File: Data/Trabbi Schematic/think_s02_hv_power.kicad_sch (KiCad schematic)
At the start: 8 parts, among them K1 Start Inhibit Relay A, M1 Main Motor AC, SW1 Battery Lock Switch, SW2 Main Current Switch, U1 Contactor Box, U2 Motor Controller (TIM)

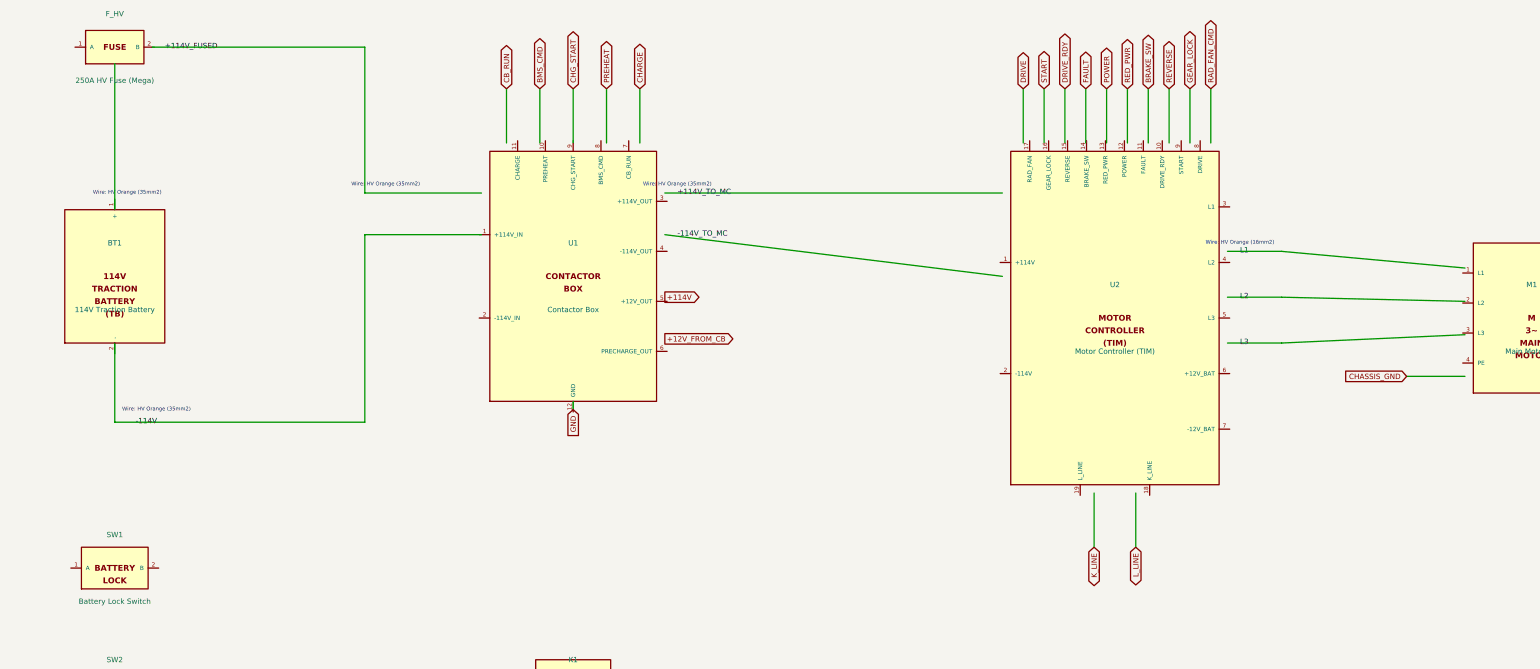
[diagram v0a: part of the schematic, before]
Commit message: Fix wire-to-pin connections: use exact calculated pin positions
Refactored gen_think_complete.py to compute exact pin schematic
coordinates instead of using approximate manual offsets. Added p()
method to Sheet class that transforms symbol-local pin positions to
schematic coordinates. All 232 wire calls across 13 sub-sheet
generators now use p() for pin endpoints, fixing misaligned
connections (previously off by 0.54-10+ units).

Co-Authored-By: Claude Opus 4.6 <noreply@anthropic.com>
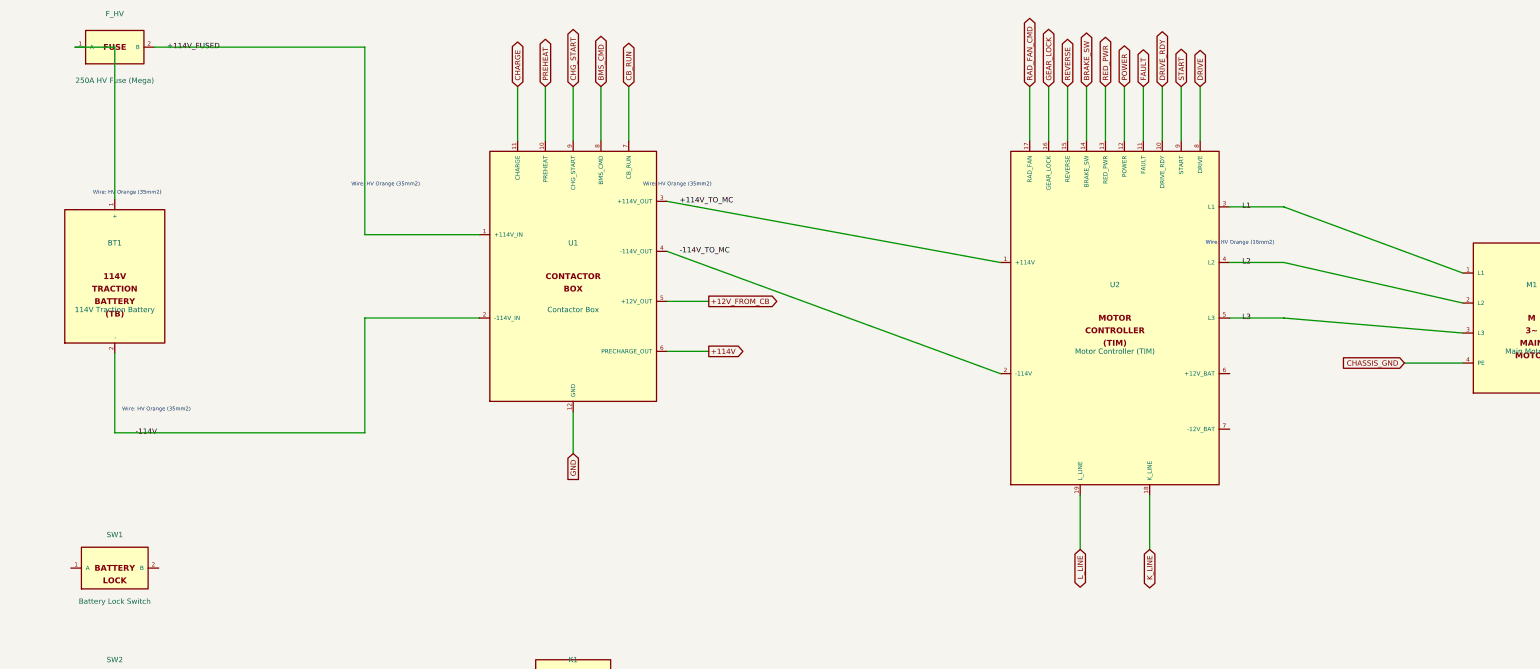
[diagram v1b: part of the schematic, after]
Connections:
- net +114V: now also U1.6 (PRECHARGE_OUT)
- net +114V_FUSED: now also F_HV.2 (B), U1.1 (+114V_IN)
- net +12V_FROM_CB: now also U1.5 (+12V_OUT)
- net -114V: now also BT1.2 (-), U1.2 (-114V_IN)
- net BMS_CMD: now also U1.8 (BMS_CMD)
- net BRAKE_SW: now also U2.14 (BRAKE_SW)
- net CB_RUN: now also U1.7 (CB_RUN)
- net CHARGE: now also U1.11 (CHARGE)
- net CHASSIS_GND: now also M1.4 (PE)
- net CHG_START: now also U1.9 (CHG_START)
- net DRIVE: now also U2.8 (DRIVE)
- net DRIVE_RDY: now also U2.10 (DRIVE_RDY)
- net FAULT: now also U2.11 (FAULT)
- net GEAR_LOCK: now also U2.16 (GEAR_LOCK)
- net GND: now also U1.12 (GND)
- net K_LINE: now also U2.18 (K_LINE)
- net L1: now also M1.1 (L1), U2.3 (L1)
- net L2: now also M1.2 (L2), U2.4 (L2)
- net L3: now also M1.3 (L3), U2.5 (L3)
- net L_LINE: now also U2.19 (L_LINE)
- net POWER: now also U2.12 (POWER)
- net PREHEAT: now also U1.10 (PREHEAT)
- net RAD_FAN_CMD: now also U2.17 (RAD_FAN)
- net RED_PWR: now also U2.13 (RED_PWR)
- net REVERSE: now also U2.15 (REVERSE)
- net START: now also U2.9 (START)
- net at F_HV.1 (A): now also BT1.1 (+)
- net at U1.3 (+114V_OUT): now also U2.1 (+114V)
- net at U1.4 (-114V_OUT): now also U2.2 (-114V)

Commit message: Enforce orthogonal routing and 1.27mm grid alignment
- Add _g() grid snap function to Sheet class (rounds all coordinates to nearest 1.27mm)
- Add wire_l() method for L-shaped orthogonal routing (horizontal+vertical segments)
- Apply grid snapping in p(), place(), wire(), label(), glabel(), junction(), no_connect(), defsym()
- Replace all 19 diagonal wire calls with wire_l() across S02, S06, S07, S08, S10, S12, S13
- All wire segments now strictly horizontal or vertical, no diagonals
- All coordinates verified on 1.27mm (50mil) KiCad standard grid

Co-Authored-By: Claude Opus 4.6 <noreply@anthropic.com>
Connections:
- net L2 is gone; now on net L1: M1.2 (L2), U2.4 (L2)
- net +114V_TO_MC: now also U1.3 (+114V_OUT), U1.4 (-114V_OUT), U2.1 (+114V), U2.2 (-114V)

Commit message: Add relay coil/switch graphics, fix label positioning
- Draw coil (inductor arcs) and switch contacts (circles + arm)
  inside RELAY_SPST and RELAY_SPDT symbol bodies
- Add body_gfx parameter to defsym() for custom symbol graphics
- Helper functions: _gfx_polyline, _gfx_arc, _gfx_circle, _relay_gfx
- Fix label offsets: increase from 3-5mm to 10-12mm to avoid
  overlapping pin names (S01 ignition, S02 HV, S05 DCDC, S07 lights)
- Fix S09 turn signal rear labels: add wire stubs (were at 0 offset)
- All 14 schematics regenerated, parentheses balanced, grid OK

Co-Authored-By: Claude Opus 4.6 <noreply@anthropic.com>
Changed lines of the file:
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@@
     (stroke (width 0) (type default))
   )
-  (label "+114V_FUSED" (at 52.070 44.450 0)
+  (label "+114V_FUSED" (at 59.690 44.450 0)
     (effects (font (size 1.27 1.27)))
   )
@@
     (stroke (width 0) (type default))
   )
-  (label "-114V" (at 44.450 138.430 0)
+  (label "-114V" (at 49.530 138.430 0)
     (effects (font (size 1.27 1.27)))
   )
@@
     (stroke (width 0) (type default))
   )
-  (label "+114V_TO_MC" (at 175.260 82.550 0)
+  (label "+114V_TO_MC" (at 182.880 82.550 0)
     (effects (font (size 1.27 1.27)))
   )
-  (label "-114V_TO_MC" (at 175.260 93.980 0)
+  (label "-114V_TO_MC" (at 182.880 93.980 0)
     (effects (font (size 1.27 1.27)))
   )
@@
     (stroke (width 0) (type default))
   )
-  (label "L1" (at 309.880 83.820 0)
+  (label "L1" (at 317.500 83.820 0)
     (effects (font (size 1.27 1.27)))
   )
@@
     (stroke (width 0) (type default))
   )
-  (label "L2" (at 309.880 97.790 0)
+  (label "L2" (at 317.500 97.790 0)
     (effects (font (size 1.27 1.27)))
   )
@@
     (stroke (width 0) (type default))
   )
-  (label "L3" (at 309.880 110.490 0)
+  (label "L3" (at 317.500 110.490 0)
     (effects (font (size 1.27 1.27)))
   )

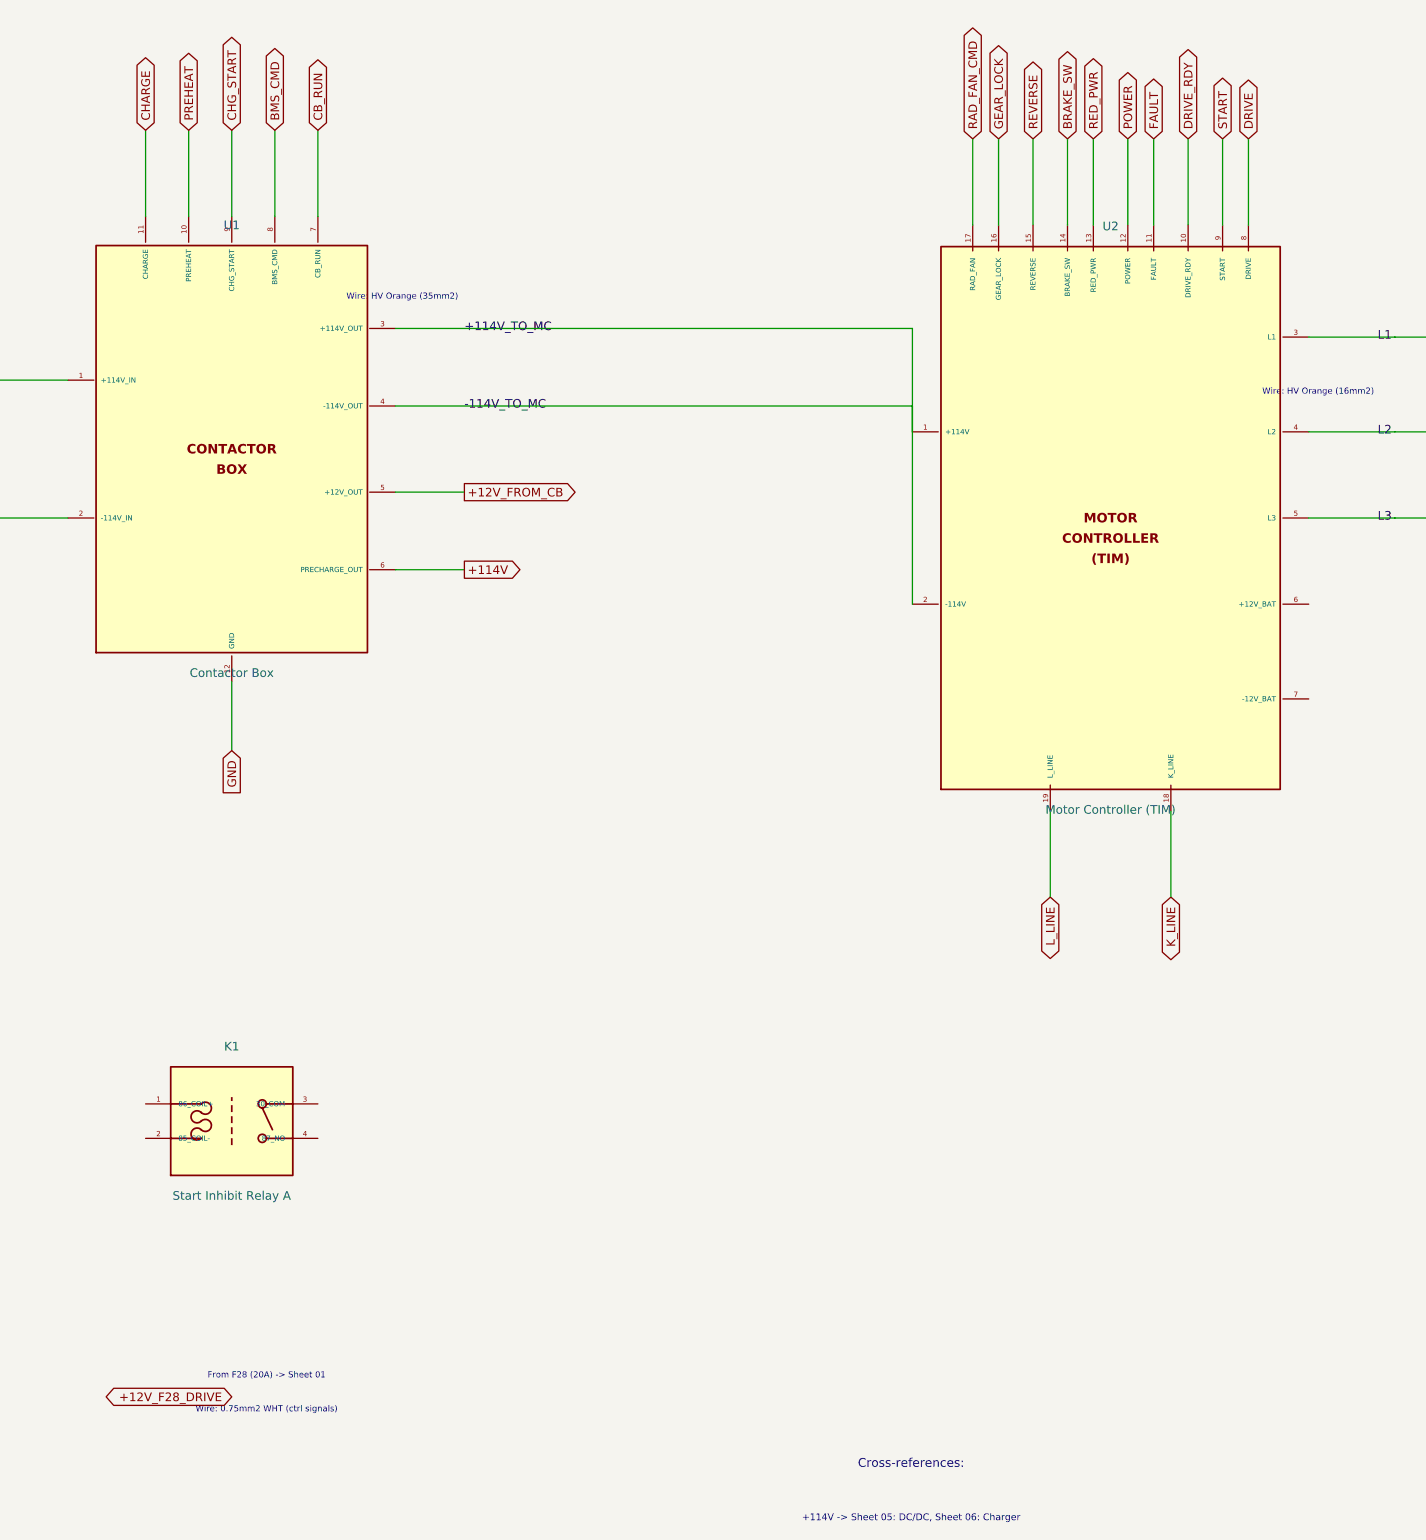
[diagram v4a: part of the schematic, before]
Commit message: Add cross-sheet reference annotations to global labels
- Track all global label positions per sheet during build
- After building all sheets, annotate each global label with
  "→S01,S03,..." text showing which other sheets share the net
- 60 cross-sheet nets identified and annotated
- Two-pass build: 1) build all sheets 2) add cross-refs + save
- Text placed near label in 0.8mm font, offset to avoid overlap

Co-Authored-By: Claude Opus 4.6 <noreply@anthropic.com>
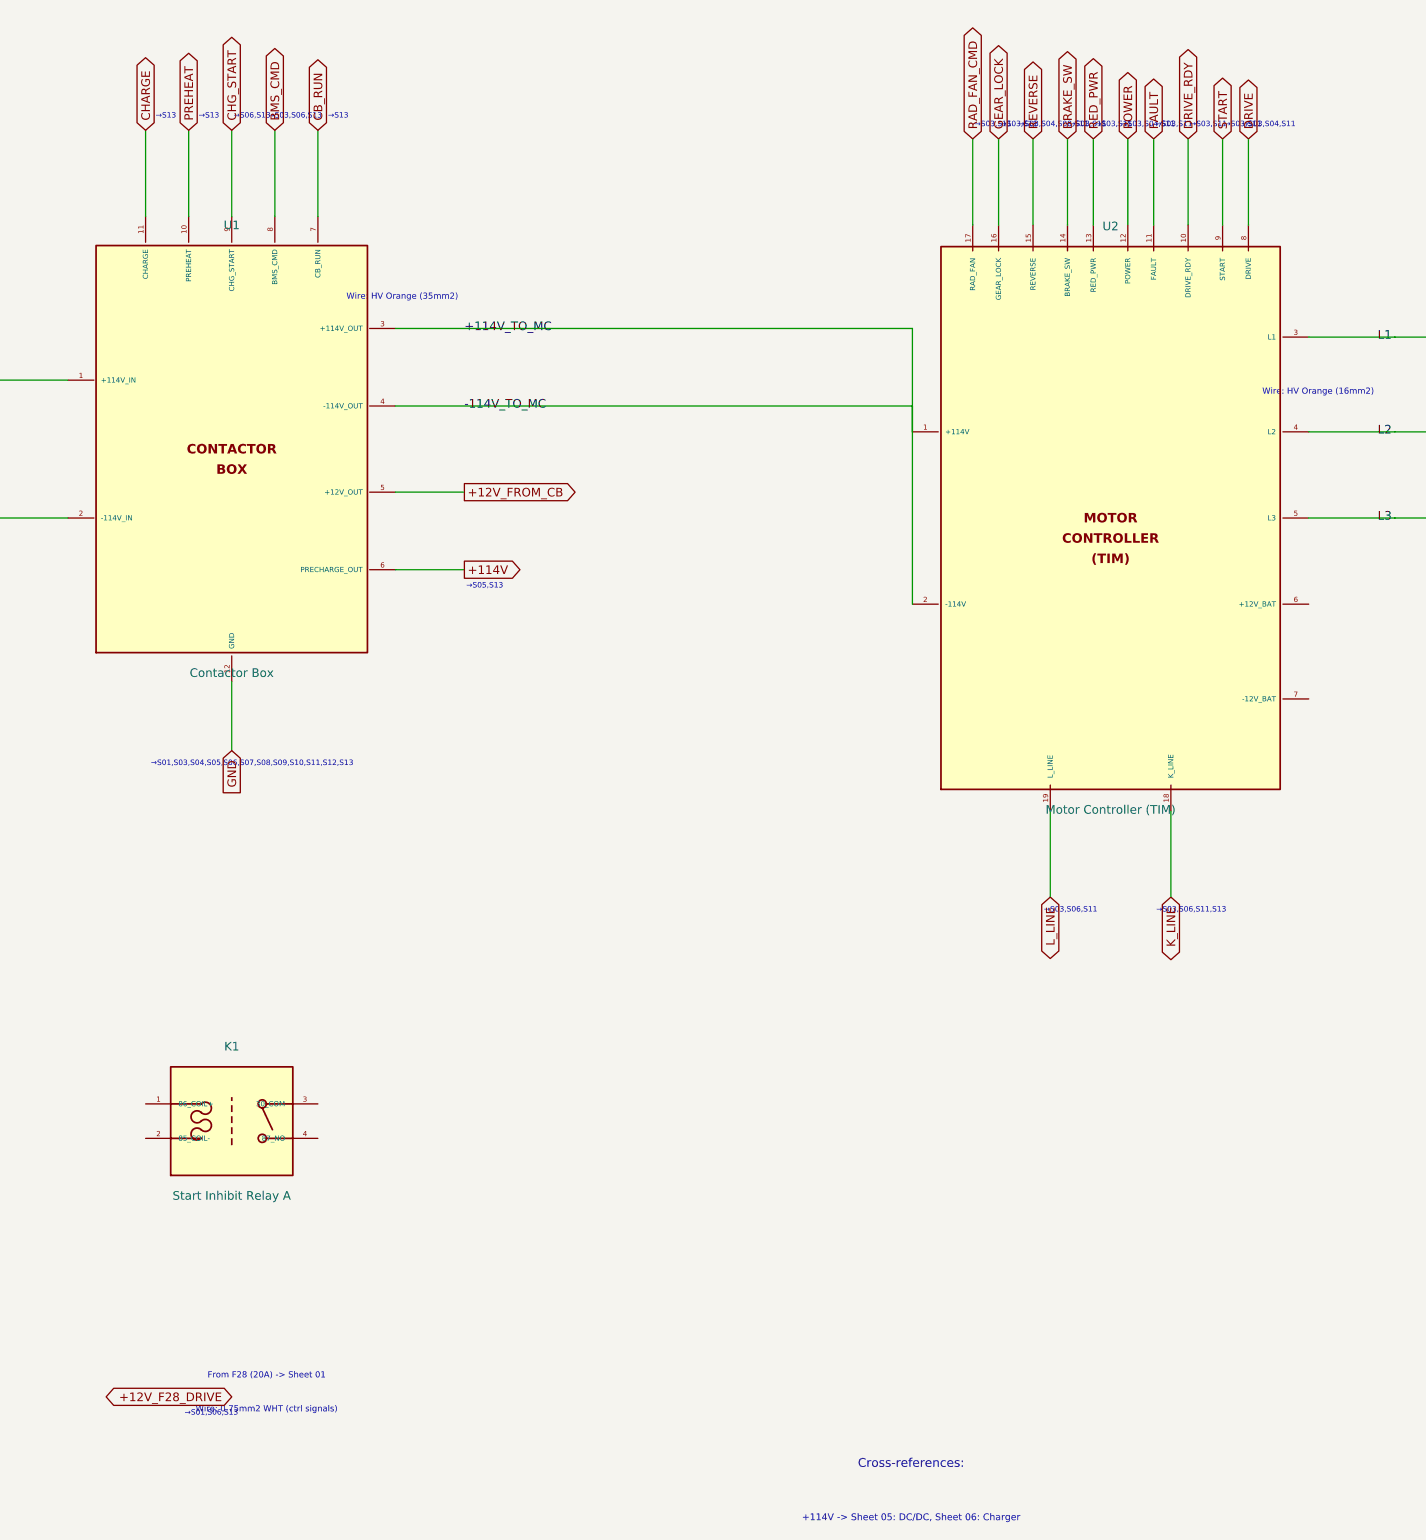
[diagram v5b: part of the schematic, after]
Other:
- note added: "→S01,S03,S04,S05,S06,S07,S08,S09,S10,S11,S12,S13"
- note added: "→S01,S06,S13"
- note added: "→S03,S04,S08,S11"
- note added: "→S03,S04,S11"
- note added: "→S03,S06,S11"
- note added: "→S03,S06,S11,S13"
- note added: "→S03,S06,S13"
- note added: "→S03,S11"
- note added: "→S05,S13"
- note added: "→S06,S13"
- note added: "→S13"
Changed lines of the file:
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@@
     (effects (font (size 1.000 1.000)))
+  )
+  (text "→S01,S03,S04,S05,S06,S07,S08,S09,S10,S11,S12,S13" (at 152.860 146.780 0)
+    (effects (font (size 0.800 0.800)))
+  )
+  (text "→S13" (at 165.560 51.340 0)
+    (effects (font (size 0.800 0.800)))
+  )
+  (text "→S03,S06,S13" (at 159.210 51.340 0)
+    (effects (font (size 0.800 0.800)))
+  )
+  (text "→S06,S13" (at 152.860 51.340 0)
+    (effects (font (size 0.800 0.800)))
+  )
+  (text "→S13" (at 146.510 51.340 0)
+    (effects (font (size 0.800 0.800)))
+  )
+  (text "→S13" (at 140.160 51.340 0)
+    (effects (font (size 0.800 0.800)))
+  )
+  (text "→S03,S04,S11" (at 302.720 52.610 0)
+    (effects (font (size 0.800 0.800)))
+  )
+  (text "→S03,S11" (at 298.910 52.610 0)
+    (effects (font (size 0.800 0.800)))
+  )
+  (text "→S03,S11" (at 293.830 52.610 0)
+    (effects (font (size 0.800 0.800)))
+  )
+  (text "→S03,S11" (at 288.750 52.610 0)
+    (effects (font (size 0.800 0.800)))
+  )
+  (text "→S03,S04,S11" (at 284.940 52.610 0)
+    (effects (font (size 0.800 0.800)))
+  )
+  (text "→S03,S11" (at 279.860 52.610 0)
+    (effects (font (size 0.800 0.800)))
+  )
+  (text "→S03,S11" (at 276.050 52.610 0)
+    (effects (font (size 0.800 0.800)))
+  )
+  (text "→S03,S04,S08,S11" (at 270.970 52.610 0)
+    (effects (font (size 0.800 0.800)))
+  )
+  (text "→S03,S11" (at 265.890 52.610 0)
+    (effects (font (size 0.800 0.800)))
+  )
+  (text "→S03,S11" (at 262.080 52.610 0)
+    (effects (font (size 0.800 0.800)))
+  )
+  (text "→S03,S06,S11,S13" (at 291.290 168.370 0)
+    (effects (font (size 0.800 0.800)))
+  )
+  (text "→S03,S06,S11" (at 273.510 168.370 0)
+    (effects (font (size 0.800 0.800)))
+  )
+  (text "→S05,S13" (at 187.150 120.610 0)
+    (effects (font (size 0.800 0.800)))
+  )
+  (text "→S01,S06,S13" (at 146.860 242.530 0)
+    (effects (font (size 0.800 0.800)))
   )
   (symbol_instances)
